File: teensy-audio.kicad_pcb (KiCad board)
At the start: 2 copper layers, 80 x 154.4 mm, 63 parts, among them J1 AudioJack3, J10 Conn_02x06_Odd_Even, J11 Conn_01x05, J12 Barrel_Jack, J13 Conn_01x04, J14 Conn_01x05, J2 Conn_01x06, J3 Conn_01x04, J4 Conn_02x05_Odd_Even, J5 AudioJack3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

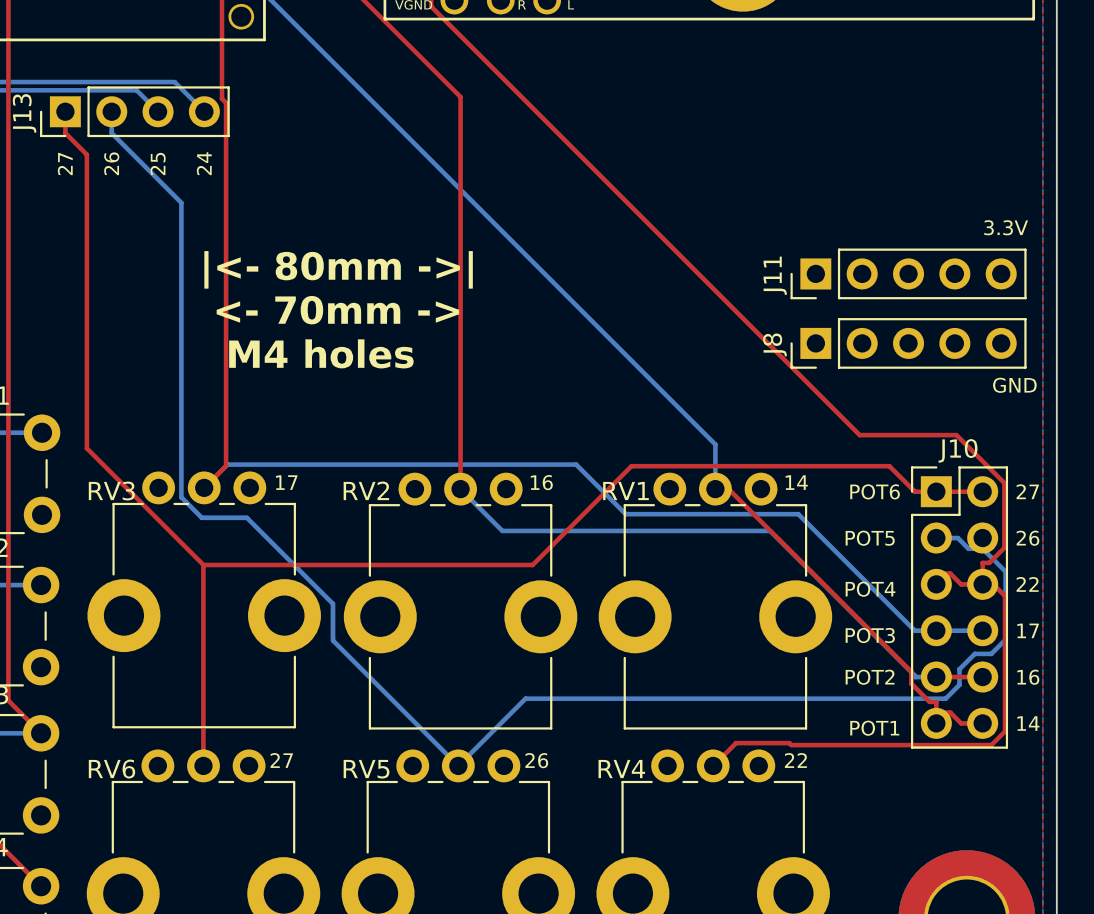
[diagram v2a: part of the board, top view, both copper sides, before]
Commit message: fix broken digital ground
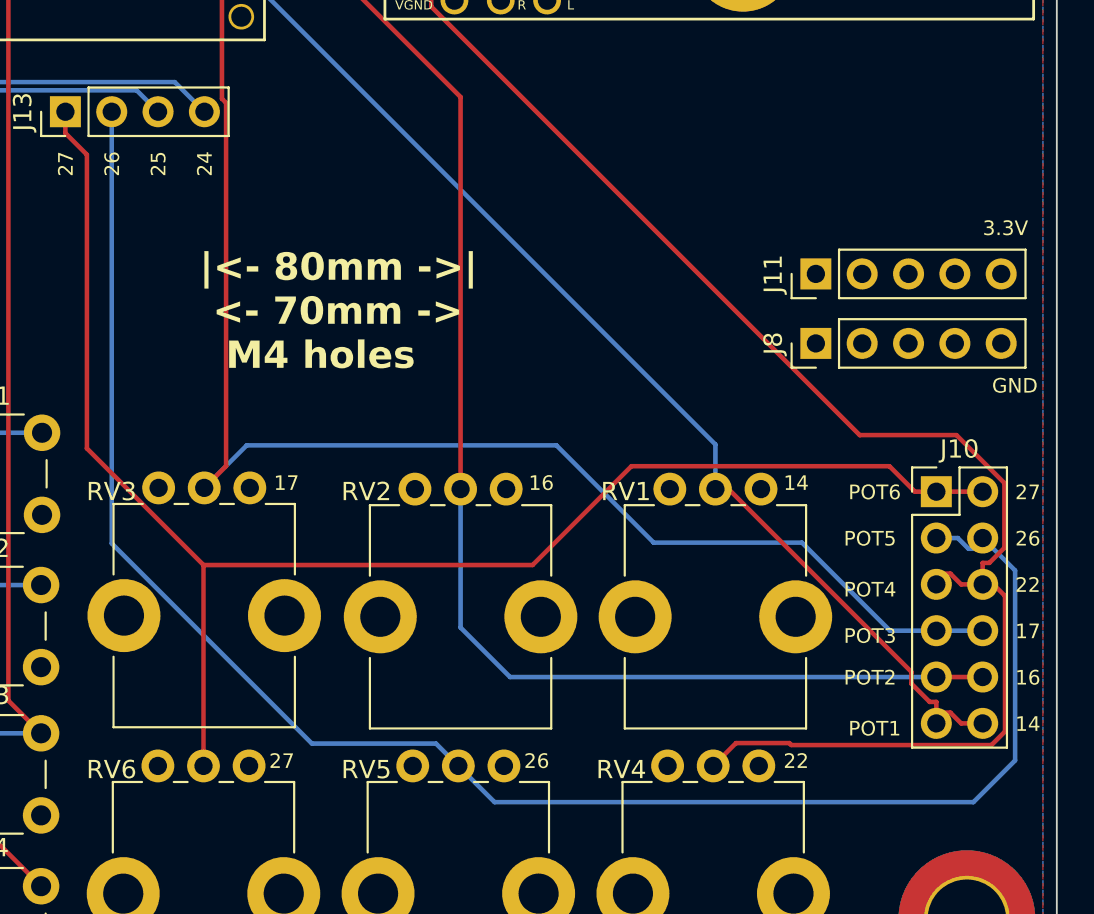
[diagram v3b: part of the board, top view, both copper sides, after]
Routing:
- net POT5: track 87.4 -> 96.3 mm
- net POT2: track 71.4 -> 75.8 mm
- net POT3: track 84.0 -> 84.9 mm
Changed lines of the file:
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@@
   (segment (start 113.366 164.45) (end 113.366 142.957) (width 0.25) (layer "F.Cu") (net 9))
   (segment (start 141.986 174.752) (end 139.446 174.752) (width 0.25) (layer "F.Cu") (net 9))
-  (segment (start 139.446 174.752) (end 138.2691 174.752) (width 0.25) (layer "B.Cu") (net 9))
-  (segment (start 138.2691 174.6784) (end 130.3312 166.7405) (width 0.25) (layer "B.Cu") (net 9))
-  (segment (start 130.3312 166.7405) (end 115.6565 166.7405) (width 0.25) (layer "B.Cu") (net 9))
-  (segment (start 115.6565 166.7405) (end 113.366 164.45) (width 0.25) (layer "B.Cu") (net 9))
-  (segment (start 138.2691 174.752) (end 138.2691 174.6784) (width 0.25) (layer "B.Cu") (net 9))
+  (segment (start 113.366 164.45) (end 113.366 172.04) (width 0.25) (layer "B.Cu") (net 9))
+  (segment (start 116.078 174.752) (end 139.446 174.752) (width 0.25) (layer "B.Cu") (net 9))
+  (segment (start 113.366 172.04) (end 116.078 174.752) (width 0.25) (layer "B.Cu") (net 9))
   (segment (start 100.2867 129.4563) (end 100.2867 143.0561) (width 0.25) (layer "F.Cu") (net 10))
   (segment (start 100.5131 163.1849) (end 99.314 164.384) (width 0.25) (layer "F.Cu") (net 10))
@@
   (segment (start 100.5131 143.2825) (end 100.5131 163.1849) (width 0.25) (layer "F.Cu") (net 10))
   (segment (start 100.2867 143.0561) (end 100.5131 143.2825) (width 0.25) (layer "F.Cu") (net 10))
-  (segment (start 119.7044 163.106) (end 122.4218 165.8234) (width 0.25) (layer "B.Cu") (net 10))
-  (segment (start 100.592 163.106) (end 119.7044 163.106) (width 0.25) (layer "B.Cu") (net 10))
-  (segment (start 122.4218 165.8234) (end 131.8805 165.8234) (width 0.25) (layer "B.Cu") (net 10))
+  (segment (start 139.446 172.212) (end 136.906 172.212) (width 0.25) (layer "B.Cu") (net 10))
   (segment (start 141.986 172.212) (end 139.446 172.212) (width 0.25) (layer "B.Cu") (net 10))
-  (segment (start 139.446 172.212) (end 138.2691 172.212) (width 0.25) (layer "B.Cu") (net 10))
-  (segment (start 131.8805 165.8234) (end 138.2691 172.212) (width 0.25) (layer "B.Cu") (net 10))
-  (segment (start 99.314 164.384) (end 100.592 163.106) (width 0.25) (layer "B.Cu") (net 10))
+  (segment (start 123.952 167.386) (end 118.618 162.052) (width 0.25) (layer "B.Cu") (net 10))
+  (segment (start 136.906 172.212) (end 132.08 167.386) (width 0.25) (layer "B.Cu") (net 10))
+  (segment (start 101.646 162.052) (end 99.314 164.384) (width 0.25) (layer "B.Cu") (net 10))
+  (segment (start 132.08 167.386) (end 123.952 167.386) (width 0.25) (layer "B.Cu") (net 10))
+  (segment (start 118.618 162.052) (end 101.646 162.052) (width 0.25) (layer "B.Cu") (net 10))
   (segment (start 141.986 169.0835) (end 143.2088 170.3063) (width 0.25) (layer "F.Cu") (net 11))
   (segment (start 141.986 169.672) (end 141.986 169.0835) (width 0.25) (layer "F.Cu") (net 11))
@@
   (segment (start 140.2206 169.0835) (end 140.8091 169.672) (width 0.25) (layer "F.Cu") (net 11))
   (segment (start 141.986 169.0835) (end 141.986 168.4951) (width 0.25) (layer "F.Cu") (net 11))
-  (segment (start 94.244 143.764) (end 94.244 144.9409) (width 0.25) (layer "B.Cu") (net 12))
-  (segment (start 98.064 164.9036) (end 98.064 148.7609) (width 0.25) (layer "B.Cu") (net 12))
-  (segment (start 140.716 175.1829) (end 139.9612 175.9377) (width 0.25) (layer "B.Cu") (net 12))
-  (segment (start 142.4658 173.482) (end 141.5551 173.482) (width 0.25) (layer "B.Cu") (net 12))
-  (segment (start 141.5551 173.482) (end 140.716 174.3211) (width 0.25) (layer "B.Cu") (net 12))
+  (segment (start 143.764 179.324) (end 141.478 181.61) (width 0.25) (layer "B.Cu") (net 12))
+  (segment (start 112.019 178.399) (end 113.244 179.624) (width 0.25) (layer "B.Cu") (net 12))
+  (segment (start 94.244 143.764) (end 94.244 167.425953) (width 0.25) (layer "B.Cu") (net 12))
+  (segment (start 115.23 181.61) (end 113.244 179.624) (width 0.25) (layer "B.Cu") (net 12))
   (segment (start 141.986 167.132) (end 141.986 167.7204) (width 0.25) (layer "B.Cu") (net 12))
   (segment (start 140.6229 167.132) (end 141.2113 167.7204) (width 0.25) (layer "B.Cu") (net 12))
-  (segment (start 101.6537 166.0236) (end 99.184 166.0236) (width 0.25) (layer "B.Cu") (net 12))
-  (segment (start 143.2425 168.9769) (end 143.2425 172.7053) (width 0.25) (layer "B.Cu") (net 12))
-  (segment (start 143.2425 172.7053) (end 142.4658 173.482) (width 0.25) (layer "B.Cu") (net 12))
-  (segment (start 106.3731 170.743) (end 101.6537 166.0236) (width 0.25) (layer "B.Cu") (net 12))
-  (segment (start 140.716 174.3211) (end 140.716 175.1829) (width 0.25) (layer "B.Cu") (net 12))
-  (segment (start 116.9303 175.9377) (end 113.244 179.624) (width 0.25) (layer "B.Cu") (net 12))
-  (segment (start 99.184 166.0236) (end 98.064 164.9036) (width 0.25) (layer "B.Cu") (net 12))
-  (segment (start 141.986 167.7204) (end 143.2425 168.9769) (width 0.25) (layer "B.Cu") (net 12))
-  (segment (start 98.064 148.7609) (end 94.244 144.9409) (width 0.25) (layer "B.Cu") (net 12))
-  (segment (start 106.3731 172.7531) (end 106.3731 170.743) (width 0.25) (layer "B.Cu") (net 12))
-  (segment (start 139.9612 175.9377) (end 116.9303 175.9377) (width 0.25) (layer "B.Cu") (net 12))
-  (segment (start 113.244 179.624) (end 106.3731 172.7531) (width 0.25) (layer "B.Cu") (net 12))
+  (segment (start 143.764 168.91) (end 143.764 179.324) (width 0.25) (layer "B.Cu") (net 12))
+  (segment (start 141.478 181.61) (end 115.23 181.61) (width 0.25) (layer "B.Cu") (net 12))
+  (segment (start 141.986 167.132) (end 143.764 168.91) (width 0.25) (layer "B.Cu") (net 12))
+  (segment (start 105.217047 178.399) (end 112.019 178.399) (width 0.25) (layer "B.Cu") (net 12))
+  (segment (start 94.244 167.425953) (end 105.217047 178.399) (width 0.25) (layer "B.Cu") (net 12))
   (segment (start 139.446 167.132) (end 140.6229 167.132) (width 0.25) (layer "B.Cu") (net 12))
   (segment (start 141.2113 167.7204) (end 141.986 167.7204) (width 0.25) (layer "B.Cu") (net 12))
